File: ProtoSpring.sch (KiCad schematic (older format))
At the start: 8 parts, among them P1 CONN_3X2, P2 CONN_7X2, P3 CONN_4X2, P4 CONN_3X2, P5 CONN_9X2, P6 CONN_4X2

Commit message: updated output
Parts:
- removed P5: CONN_9X2, ~, symbol CONN_9X2
- added C1, C3: 0.1u, ~, symbol C
- added C2, C4: 10u, ~, symbol CP1
- added D1: LED, ~, symbol LED
- added P10, P11, P12, P13, P14, P15, P16, P17, P18, P19, P20, P21, P22, P23, P24, P25, P26, P27, P8, P9: CONN_14, ~, symbol CONN_14
- added P5: CONN_8X2, ~, symbol CONN_8X2
- added P6: CONN_2X2, ~, symbol CONN_2X2
- added R1: 390, ~, symbol R
- P1: Mouser# (none) -> 517-950406-5002-AR; Part# (none) -> 950406-5002-AR
- P2: Mouser# (none) -> 517-950414-5002-AR; Part# (none) -> 950414-5002-AR
- P3: Mouser# (none) -> 517-950408-5002-AR; Part# (none) -> 950408-5002-AR
- renumbered P6 to P7
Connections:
- wire segments 4 -> 51
- no-connect marks 1 -> 2
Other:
- note added: "Breadboard pins"
- note added: "Pin numbers not direct equivalent to ones on Springboard\nNeed to flip them for orientation"
- moved on the sheet: F1, F2, P1, P2, P3, P4, P7

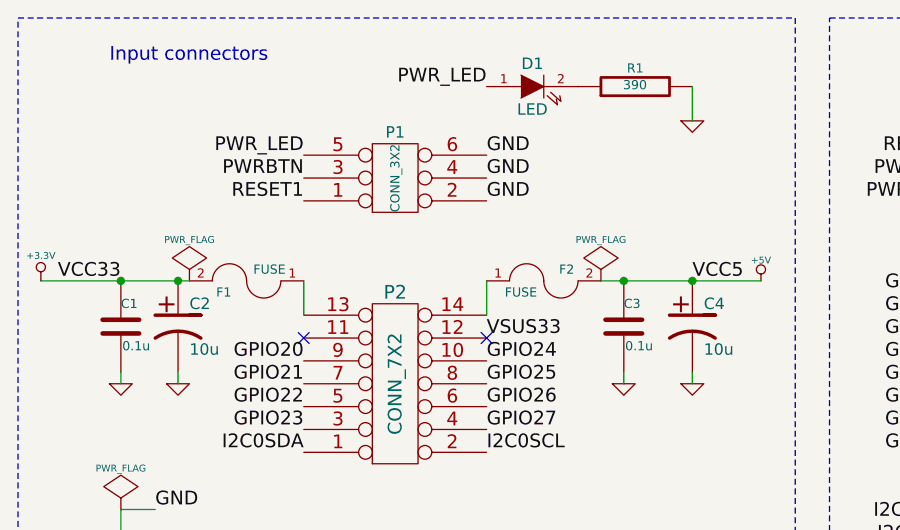
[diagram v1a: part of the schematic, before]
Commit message: update schematics and pcb with some lessons learned
Brief changelog:

* add manufacturers and part numbers for recommended parts
* change current limiting resistor for LED to fit its current requirements
* update PCB with new resistor value
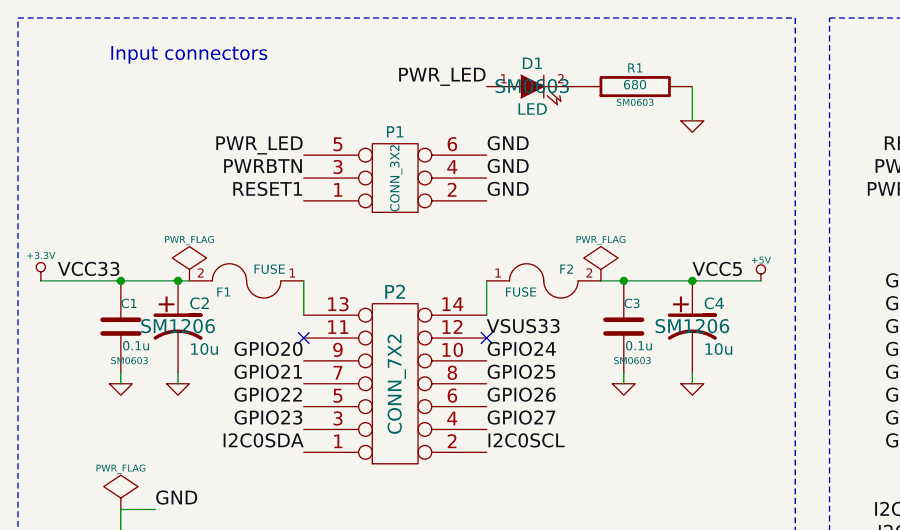
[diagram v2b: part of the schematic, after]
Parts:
- C1, C3: footprint ~ -> SM0603; Manufacturer (none) -> AVX; PartNumber (none) -> 0603YC104KAT2A
- C2, C4: footprint ~ -> SM1206; Manufacturer (none) -> AVX; PartNumber (none) -> F931A106KAA
- D1: footprint ~ -> SM0603; Manufacturer (none) -> Osram; Mouser# 720-LBQ39GL2N2351 -> (none); Part# LB Q39G-L2N2-35-1 -> (none); PartNumber (none) -> LB Q39G-L2N2-35-1
- F1, F2: Manufacturer (none) -> Littelfuse; PartNumber (none) -> 1206L110THYR; Seeed PN 0900030P1 -> (none)
- P1: Manufacturer (none) -> 3M; Mouser# 517-950406-5002-AR -> (none)
- P2: Manufacturer (none) -> 3M; Mouser# 517-950414-5002-AR -> (none)
- P3: Manufacturer (none) -> 3M; Mouser# 517-950408-5002-AR -> (none)
- R1: value 390 -> 680; footprint ~ -> SM0603; Manufacturer (none) -> Vishay; Mouser# 71-CRCW0603-390-E3 -> (none); Part# CRCW0603390RFKEA -> CRCW0603680RFKEA
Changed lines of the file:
@@
 Sheet 1 1
 Title "ProtoSpring for VAB-600 Springboard"
-Date "28 oct 2014"
+Date "9 nov 2014"
 Rev "v1"
 Comp "VIA Embedded / Gergely Imreh"
@@
 F 3 "~" H 2350 1250 60  0000 C CNN
 F 4 "950406-5002-AR" H 2350 1250 60  0001 C CNN "Part#"
-F 5 "517-950406-5002-AR" H 2350 1250 60  0001 C CNN "Mouser#"
+F 5 "3M" H 2350 1250 60  0001 C CNN "Manufacturer"
 	1    2350 1250
 	1    0    0    1
@@
 F 3 "~" H 2350 2200 60  0000 C CNN
 F 4 "950414-5002-AR" H 2350 2200 60  0001 C CNN "Part#"
-F 5 "517-950414-5002-AR" H 2350 2200 60  0001 C CNN "Mouser#"
+F 5 "3M" H 2350 2200 60  0001 C CNN "Manufacturer"
 	1    2350 2200
 	1    0    0    1
@@
 F 3 "~" H 2350 3200 60  0000 C CNN
 F 4 "950408-5002-AR" H 2350 3200 60  0001 C CNN "Part#"
-F 5 "517-950408-5002-AR" H 2350 3200 60  0001 C CNN "Mouser#"
+F 5 "3M" H 2350 3200 60  0001 C CNN "Manufacturer"
 	1    2350 3200
 	1    0    0    1
@@
 F 2 "SMD1206" H 3000 1750 60  0001 C CNN
 F 3 "~" H 3000 1750 60  0000 C CNN
-F 4 "0900030P1" H 3000 1750 60  0001 C CNN "Seeed PN"
+F 4 "1206L110THYR" H 3000 1750 60  0001 C CNN "PartNumber"
+F 5 "Littelfuse" H 3000 1750 60  0001 C CNN "Manufacturer"
 	1    3000 1750
 	1    0    0    -1
@@
 F 2 "SMD1206" H 1850 1850 60  0001 C CNN
 F 3 "~" H 1700 1750 60  0000 C CNN
-F 4 "0900030P1" H 1700 1750 60  0001 C CNN "Seeed PN"
+F 4 "1206L110THYR" H 1700 1750 60  0001 C CNN "PartNumber"
+F 5 "Littelfuse" H 1700 1750 60  0001 C CNN "Manufacturer"
 	1    1700 1750
 	-1   0    0    1
@@
 F 0 "C4" H 3700 2050 50  0000 L CNN
 F 1 "10u" H 3700 1850 50  0000 L CNN
-F 2 "~" H 3650 1950 60  0000 C CNN
+F 2 "SM1206" H 3650 1950 60  0000 C CNN
 F 3 "~" H 3650 1950 60  0000 C CNN
+F 4 "F931A106KAA" H 3650 1950 60  0001 C CNN "PartNumber"
+F 5 "AVX" H 3650 1950 60  0001 C CNN "Manufacturer"
 	1    3650 1950
 	1    0    0    -1
@@
 F 0 "C2" H 1450 2050 50  0000 L CNN
 F 1 "10u" H 1450 1850 50  0000 L CNN
-F 2 "~" H 1400 1950 60  0000 C CNN
+F 2 "SM1206" H 1400 1950 60  0000 C CNN
 F 3 "~" H 1400 1950 60  0000 C CNN
+F 4 "F931A106KAA" H 1400 1950 60  0001 C CNN "PartNumber"
+F 5 "AVX" H 1400 1950 60  0001 C CNN "Manufacturer"
 	1    1400 1950
 	1    0    0    -1
@@
 F 0 "C1" H 1150 2050 40  0000 L CNN
 F 1 "0.1u" H 1156 1865 40  0000 L CNN
-F 2 "~" H 1188 1800 30  0000 C CNN
+F 2 "SM0603" H 1188 1800 30  0000 C CNN
 F 3 "~" H 1150 1950 60  0000 C CNN
+F 4 "0603YC104KAT2A" H 1150 1950 60  0001 C CNN "PartNumber"
+F 5 "AVX" H 1150 1950 60  0001 C CNN "Manufacturer"
 	1    1150 1950
 	1    0    0    -1
@@
 F 0 "C3" H 3350 2050 40  0000 L CNN
 F 1 "0.1u" H 3356 1865 40  0000 L CNN
-F 2 "~" H 3388 1800 30  0000 C CNN
+F 2 "SM0603" H 3388 1800 30  0000 C CNN
 F 3 "~" H 3350 1950 60  0000 C CNN
+F 4 "0603YC104KAT2A" H 3350 1950 60  0001 C CNN "PartNumber"
+F 5 "AVX" H 3350 1950 60  0001 C CNN "Manufacturer"
 	1    3350 1950
 	1    0    0    -1
@@
 F 0 "D1" H 2950 1000 50  0000 C CNN
 F 1 "LED" H 2950 800 50  0000 C CNN
-F 2 "~" H 2950 900 60  0000 C CNN
+F 2 "SM0603" H 2950 900 60  0000 C CNN
 F 3 "~" H 2950 900 60  0000 C CNN
-F 4 "LB Q39G-L2N2-35-1" H 2950 900 60  0001 C CNN "Part#"
-F 5 "720-LBQ39GL2N2351" H 2950 900 60  0001 C CNN "Mouser#"
+F 4 "LB Q39G-L2N2-35-1" H 2950 900 60  0001 C CNN "PartNumber"
+F 5 "Osram" H 2950 900 60  0001 C CNN "Manufacturer"
 	1    2950 900
 	1    0    0    -1
@@
 P 3400 900
 F 0 "R1" V 3480 900 40  0000 C CNN
-F 1 "390" V 3407 901 40  0000 C CNN
-F 2 "~" V 3330 900 30  0000 C CNN
+F 1 "680" V 3407 901 40  0000 C CNN
+F 2 "SM0603" V 3330 900 30  0000 C CNN
 F 3 "~" H 3400 900 30  0000 C CNN
-F 4 "CRCW0603390RFKEA" V 3400 900 60  0001 C CNN "Part#"
-F 5 "71-CRCW0603-390-E3" V 3400 900 60  0001 C CNN "Mouser#"
+F 4 "CRCW0603680RFKEA" V 3400 900 60  0001 C CNN "Part#"
+F 5 "Vishay" V 3400 900 60  0001 C CNN "Manufacturer"
 	1    3400 900
 	0    -1   -1   0

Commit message: latest changes
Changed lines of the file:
@@
 Sheet 1 1
 Title "ProtoSpring for VAB-600 Springboard"
-Date "9 nov 2014"
+Date "26 jun 2015"
 Rev "v1"
 Comp "VIA Embedded / Gergely Imreh"
@@
 F 0 "C4" H 3700 2050 50  0000 L CNN
 F 1 "10u" H 3700 1850 50  0000 L CNN
-F 2 "SM1206" H 3650 1950 60  0000 C CNN
+F 2 "SM1206" H 3650 1950 60  0001 C CNN
 F 3 "~" H 3650 1950 60  0000 C CNN
 F 4 "F931A106KAA" H 3650 1950 60  0001 C CNN "PartNumber"
@@
 F 0 "C2" H 1450 2050 50  0000 L CNN
 F 1 "10u" H 1450 1850 50  0000 L CNN
-F 2 "SM1206" H 1400 1950 60  0000 C CNN
+F 2 "SM1206" H 1400 1950 60  0001 C CNN
 F 3 "~" H 1400 1950 60  0000 C CNN
 F 4 "F931A106KAA" H 1400 1950 60  0001 C CNN "PartNumber"
@@
 F 0 "C1" H 1150 2050 40  0000 L CNN
 F 1 "0.1u" H 1156 1865 40  0000 L CNN
-F 2 "SM0603" H 1188 1800 30  0000 C CNN
+F 2 "SM0603" H 1188 1800 30  0001 C CNN
 F 3 "~" H 1150 1950 60  0000 C CNN
 F 4 "0603YC104KAT2A" H 1150 1950 60  0001 C CNN "PartNumber"
@@
 F 0 "C3" H 3350 2050 40  0000 L CNN
 F 1 "0.1u" H 3356 1865 40  0000 L CNN
-F 2 "SM0603" H 3388 1800 30  0000 C CNN
+F 2 "SM0603" H 3388 1800 30  0001 C CNN
 F 3 "~" H 3350 1950 60  0000 C CNN
 F 4 "0603YC104KAT2A" H 3350 1950 60  0001 C CNN "PartNumber"
@@
 F 0 "D1" H 2950 1000 50  0000 C CNN
 F 1 "LED" H 2950 800 50  0000 C CNN
-F 2 "SM0603" H 2950 900 60  0000 C CNN
+F 2 "SM0603" H 2950 900 60  0001 C CNN
 F 3 "~" H 2950 900 60  0000 C CNN
 F 4 "LB Q39G-L2N2-35-1" H 2950 900 60  0001 C CNN "PartNumber"
@@
 F 0 "R1" V 3480 900 40  0000 C CNN
 F 1 "680" V 3407 901 40  0000 C CNN
-F 2 "SM0603" V 3330 900 30  0000 C CNN
+F 2 "SM0603" V 3330 900 30  0001 C CNN
 F 3 "~" H 3400 900 30  0000 C CNN
 F 4 "CRCW0603680RFKEA" V 3400 900 60  0001 C CNN "Part#"
